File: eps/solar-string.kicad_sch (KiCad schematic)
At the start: 4 parts, among them J1 Conn_01x02

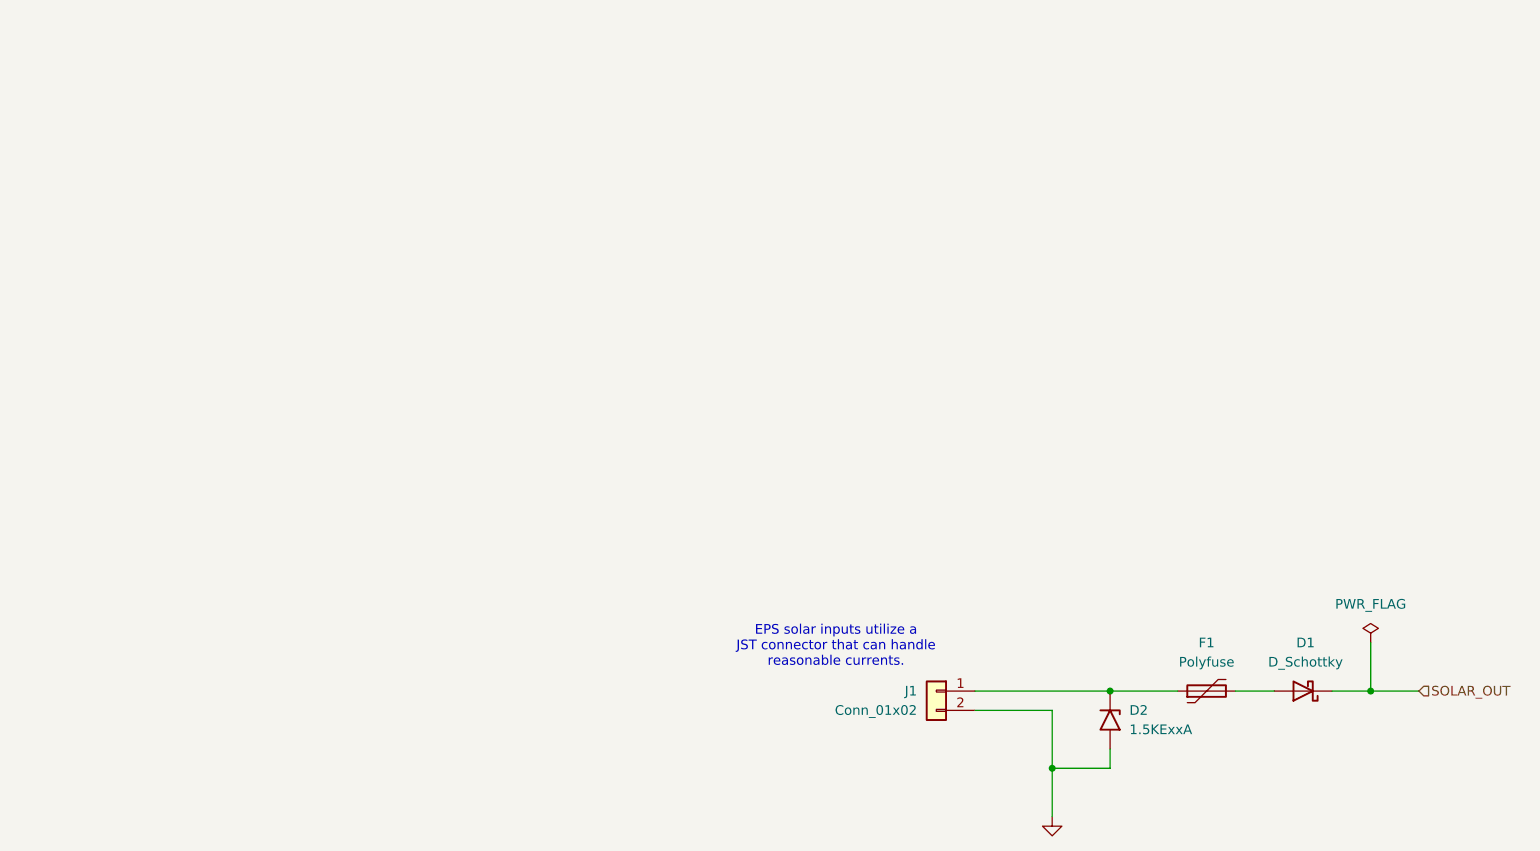
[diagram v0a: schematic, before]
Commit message: add LTC3130 buck-boost MPPT controller and connect solar strings
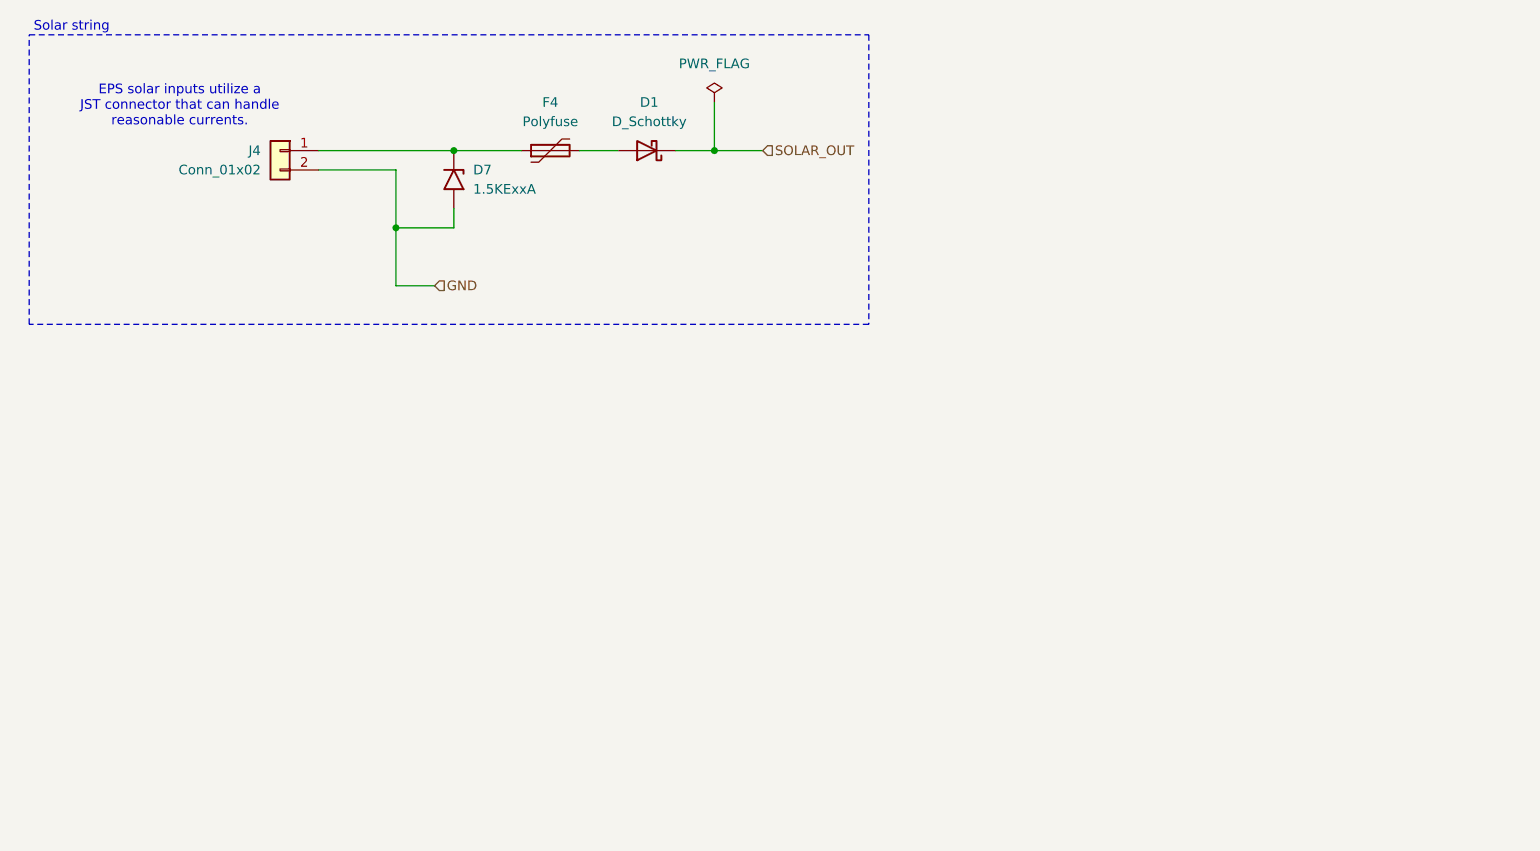
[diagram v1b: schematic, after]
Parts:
- renumbered D2 to D7, F1 to F4, J1 to J4
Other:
- note added: "Solar string"
- moved on the sheet: D1, D7, F4, J4

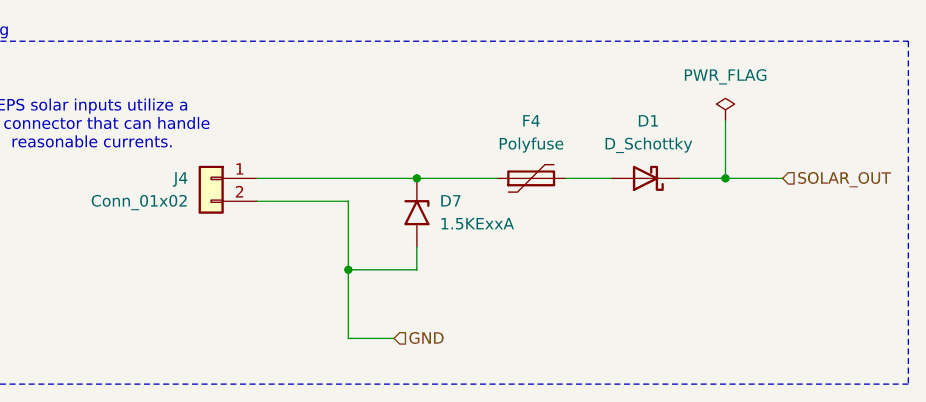
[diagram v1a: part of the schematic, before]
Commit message: add battery charger
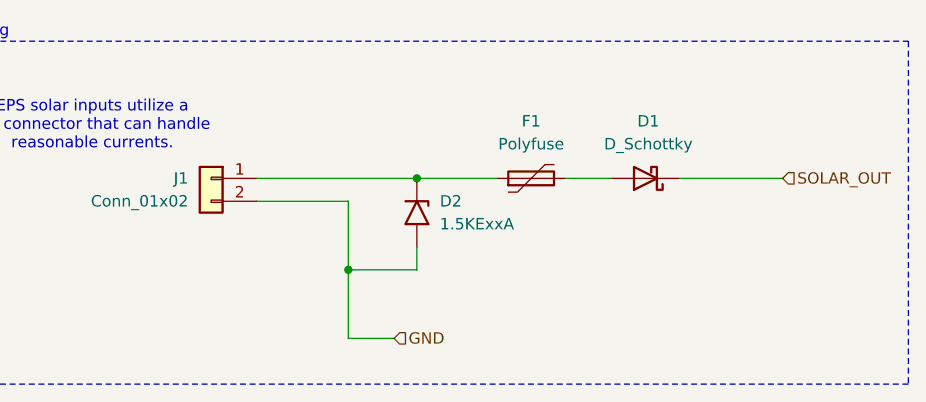
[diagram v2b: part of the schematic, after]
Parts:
- renumbered D7 to D2, F4 to F1, J4 to J1
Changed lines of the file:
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@@
 		(color 0 0 0 0)
 	)
-	(junction
-		(at 104.14 30.48)
-		(diameter 0)
-		(color 0 0 0 0)
+	(wire
+		(pts
+			(xy 52.07 30.48) (xy 69.85 30.48)
+		)
+		(stroke
+			(width 0)
+			(type default)
+		)
 	)
 	(wire
@@
 	(wire
 		(pts
-			(xy 104.14 24.13) (xy 104.14 30.48)
-		)
-		(stroke
-			(width 0)
-			(type default)
-		)
-	)
-	(wire
-		(pts
 			(xy 69.85 38.1) (xy 69.85 40.64)
 		)
@@
 	(wire
 		(pts
-			(xy 99.06 30.48) (xy 104.14 30.48)
+			(xy 99.06 30.48) (xy 110.49 30.48)
 		)
 		(stroke
@@
 	(wire
 		(pts
-			(xy 104.14 30.48) (xy 110.49 30.48)
-		)
-		(stroke
-			(width 0)
-			(type default)
-		)
-	)
-	(wire
-		(pts
 			(xy 62.23 33.02) (xy 62.23 40.64)
 		)
@@
 		(pts
 			(xy 69.85 40.64) (xy 62.23 40.64)
-		)
-		(stroke
-			(width 0)
-			(type default)
-		)
-	)
-	(wire
-		(pts
-			(xy 52.07 30.48) (xy 69.85 30.48)
 		)
 		(stroke
@@
 			)
 			(justify left)
-		)
-	)
-	(symbol
-		(lib_id "power:PWR_FLAG")
-		(at 104.14 24.13 0)
-		(unit 1)
-		(exclude_from_sim no)
-		(in_bom yes)
-		(on_board yes)
-		(dnp no)
-		(fields_autoplaced yes)
-		(property "Reference" "#FLG?"
-			(at 104.14 22.225 0)
-			(effects
-				(font
-					(size 1.27 1.27)
-				)
-				(hide yes)
-			)
-		)
-		(property "Value" "PWR_FLAG"
-			(at 104.14 19.05 0)
-			(effects
-				(font
-					(size 1.27 1.27)
-				)
-			)
-		)
-		(property "Footprint" ""
-			(at 104.14 24.13 0)
-			(effects
-				(font
-					(size 1.27 1.27)
-				)
-				(hide yes)
-			)
-		)
-		(property "Datasheet" "~"
-			(at 104.14 24.13 0)
-			(effects
-				(font
-					(size 1.27 1.27)
-				)
-				(hide yes)
-			)
-		)
-		(property "Description" "Special symbol for telling ERC where power comes from"
-			(at 104.14 24.13 0)
-			(effects
-				(font
-					(size 1.27 1.27)
-				)
-				(hide yes)
-			)
-		)
-		(pin "1"
-		)
-		(instances
-			(project "eps"
-				(path "/9e0ae2e7-d4be-41b4-8312-0d2aceea2180/342a7a20-d9c6-42fd-a259-f94205f4db38"
-					(reference "#FLG04")
-					(unit 1)
-				)
-				(path "/9e0ae2e7-d4be-41b4-8312-0d2aceea2180/4257469c-2348-41eb-9f87-799be927b275"
-					(reference "#FLG02")
-					(unit 1)
-				)
-				(path "/9e0ae2e7-d4be-41b4-8312-0d2aceea2180/781050f4-02b6-4464-97f8-ed05cdd43c71"
-					(reference "#FLG06")
-					(unit 1)
-				)
-				(path "/9e0ae2e7-d4be-41b4-8312-0d2aceea2180/7f2ac21e-c948-4961-b937-3ff4ba7ed83e"
-					(reference "#FLG05")
-					(unit 1)
-				)
-				(path "/9e0ae2e7-d4be-41b4-8312-0d2aceea2180/8656506a-f3cd-4e75-b5fa-6b385f9fb82d"
-					(reference "#FLG?")
-					(unit 1)
-				)
-				(path "/9e0ae2e7-d4be-41b4-8312-0d2aceea2180/bd55b334-e215-4ca4-9539-708858ff2e9b"
-					(reference "#FLG03")
-					(unit 1)
-				)
-			)
 		)
 	)
@@
 		(dnp no)
 		(fields_autoplaced yes)
-		(property "Reference" "F?"
+		(property "Reference" "F1"
 			(at 82.55 24.13 90)
 			(effects
@@
 				)
 				(path "/9e0ae2e7-d4be-41b4-8312-0d2aceea2180/8656506a-f3cd-4e75-b5fa-6b385f9fb82d"
-					(reference "F?")
+					(reference "F1")
 					(unit 1)
 				)
@@
 		(on_board yes)
 		(dnp no)
-		(property "Reference" "J?"
+		(property "Reference" "J1"
 			(at 44.45 30.4799 0)
 			(effects
@@
 				)
 				(path "/9e0ae2e7-d4be-41b4-8312-0d2aceea2180/8656506a-f3cd-4e75-b5fa-6b385f9fb82d"
-					(reference "J?")
+					(reference "J1")
 					(unit 1)
 				)
@@
 		(dnp no)
 		(fields_autoplaced yes)
-		(property "Reference" "D?"
+		(property "Reference" "D2"
 			(at 72.39 33.0199 90)
 			(effects
@@
 				)
 				(path "/9e0ae2e7-d4be-41b4-8312-0d2aceea2180/8656506a-f3cd-4e75-b5fa-6b385f9fb82d"
-					(reference "D?")
-					(unit 1)
-				)
+					(reference "D2")
+					(unit 1)
+				)
